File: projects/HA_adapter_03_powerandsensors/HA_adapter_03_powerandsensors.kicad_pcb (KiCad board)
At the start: 2 copper layers, 52.1 x 31.7 mm, 15 parts, among them J1 TerminalBlock_2pin, J2 TerminalBlock_2pin, J3 TerminalBlock_3pin, J4 TerminalBlock_2pin, J5 TerminalBlock_3pin, J6 TerminalBlock_3pin, J7 TerminalBlock_3pin, J8 TerminalBlock_3pin, J9 TerminalBlock_3pin, T1 HA_adapter_03_powerandsensors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

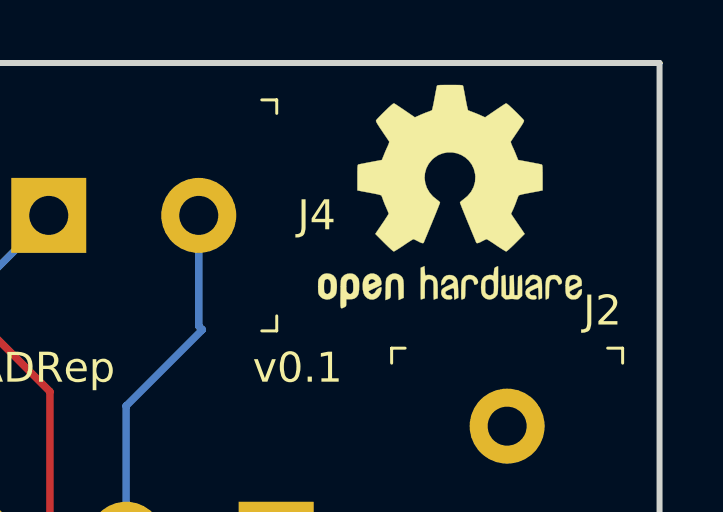
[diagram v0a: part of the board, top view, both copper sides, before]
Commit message: snapshot prior to changing HA_ESP8266_01 (removing 3pin for one IO and adding 4k7 for dallas 18b20 sensor)
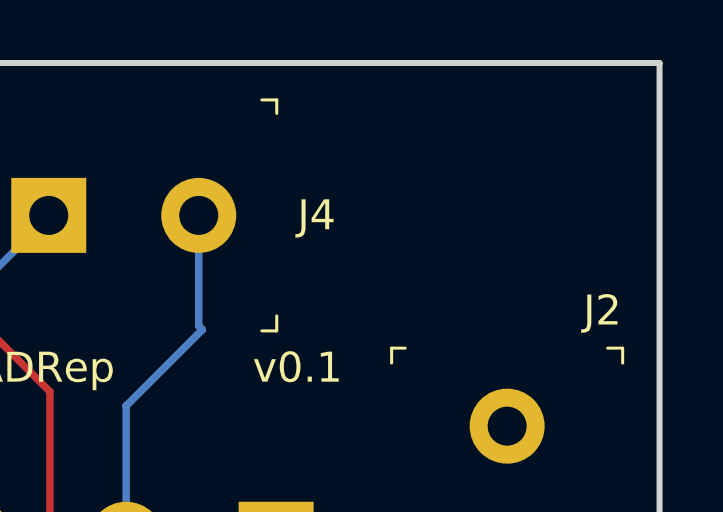
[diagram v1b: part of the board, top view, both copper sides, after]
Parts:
- removed REF**: OSHW-Logo2_9.8x8mm_SilkScreen, UH_Symbol:OSHW-Logo2_9.8x8mm_SilkScreen
- T5: footprint UH_HA:JLCJLCJLCJLC -> UH_HA:PCB_Version
- moved T5 50.8 mm to (134.0, 75.6), turned to -90 degrees

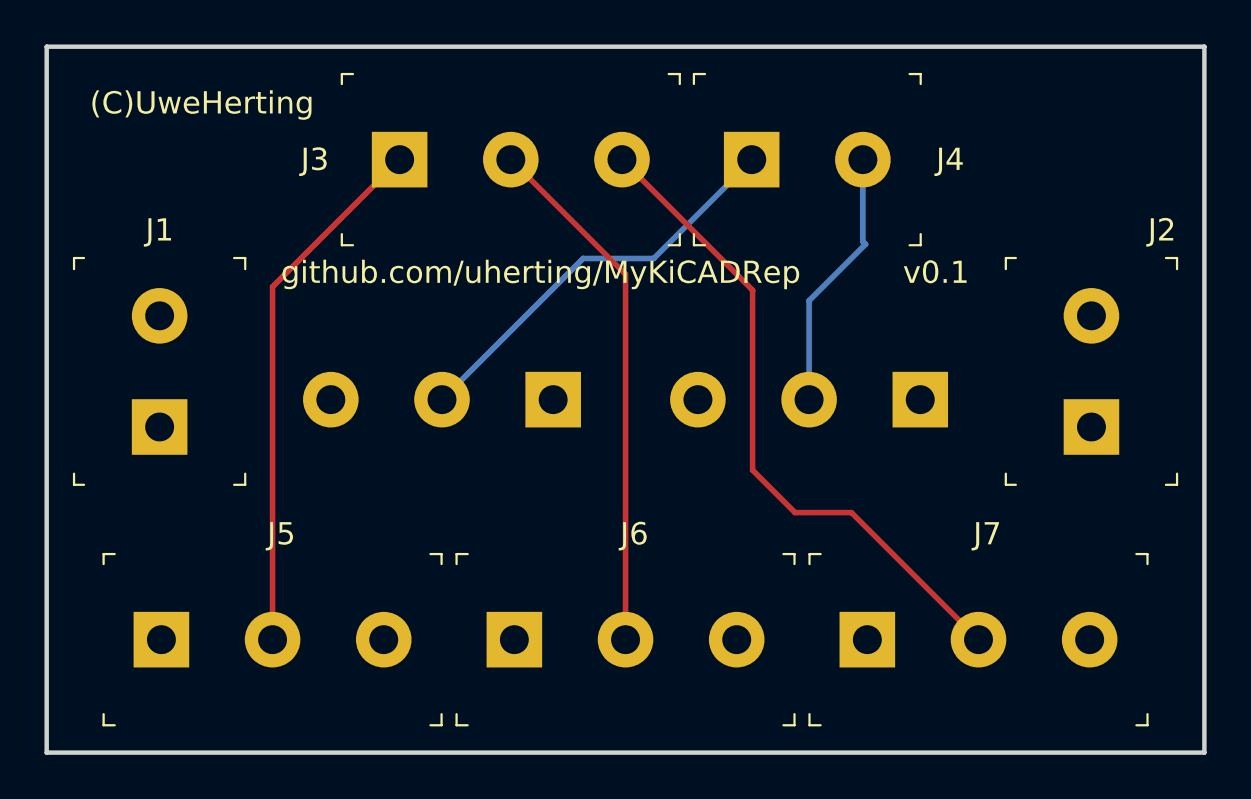
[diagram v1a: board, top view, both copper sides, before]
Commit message: updated projects HA_OPTO_COUPLER_03 and HA_adapter_03_powerandsensors
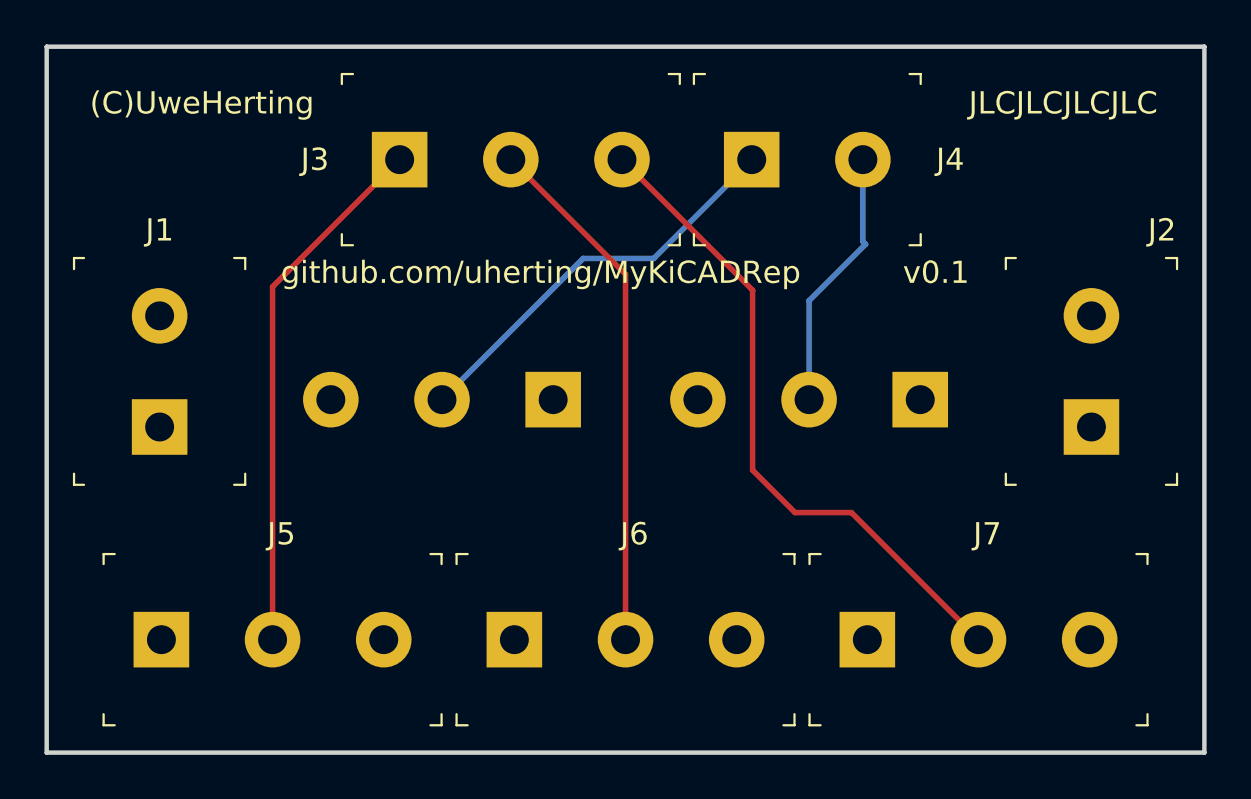
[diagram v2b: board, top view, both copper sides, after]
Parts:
- T5: moved to F.Cu
- moved T5 12.2 mm to (128.3, 64.8), turned to 0 degrees
